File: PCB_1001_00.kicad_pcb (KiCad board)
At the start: 2 copper layers, 37.6 x 30.7 mm, 4 parts, among them SW1 SW_MEC_5G

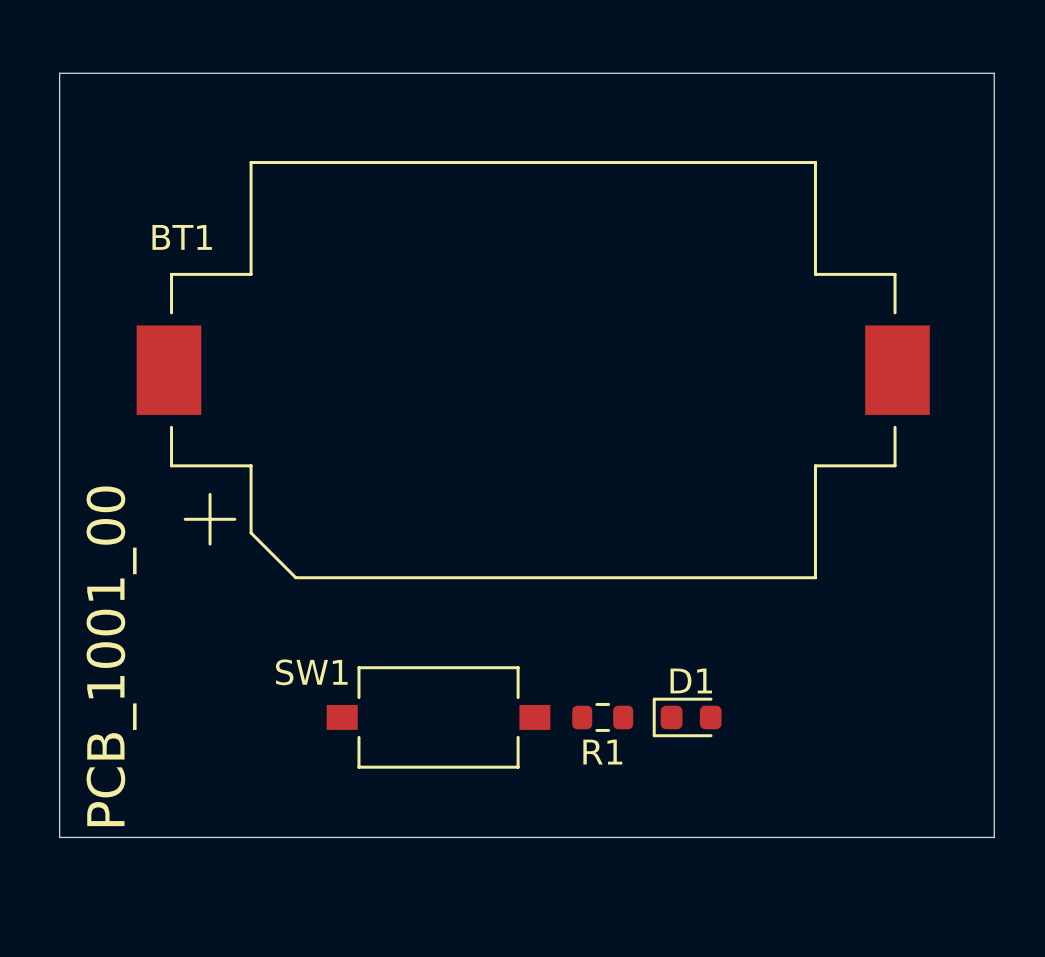
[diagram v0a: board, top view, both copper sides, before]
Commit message: PCB -->01, 2 additional LED circuits
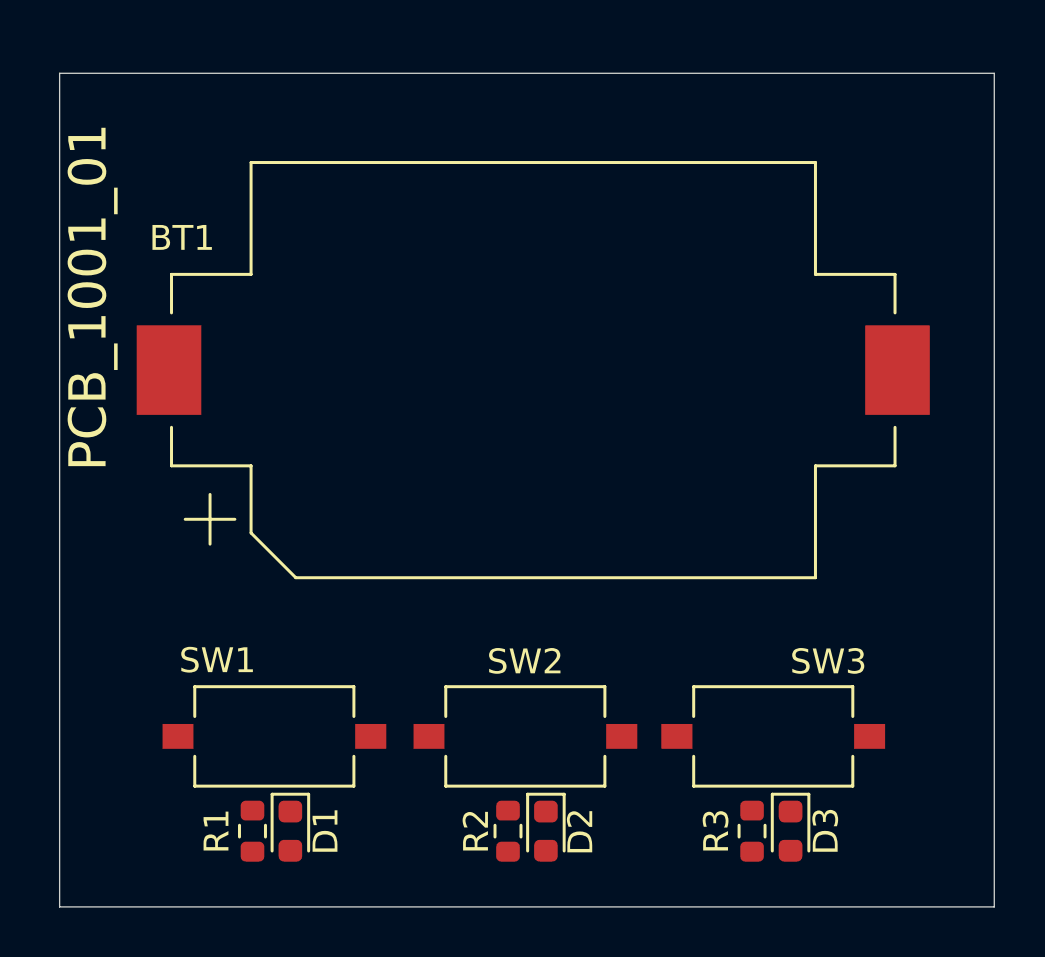
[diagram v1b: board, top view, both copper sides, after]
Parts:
- added D2: LED, LED_SMD:LED_0603_1608Metric, F.Cu at (143.3, 109.0)
- added D3: LED, LED_SMD:LED_0603_1608Metric, F.Cu at (153.1, 109.0)
- added R2: 330R, Resistor_SMD:R_0603_1608Metric, F.Cu at (141.7, 109.0)
- added R3: 330R, Resistor_SMD:R_0603_1608Metric, F.Cu at (151.5, 109.0)
- added SW2: SW_MEC_5G, Button_Switch_SMD:SW_Tactile_SPST_NO_Straight_CK_PTS636Sx25SMTRLFS, F.Cu at (142.4, 105.2)
- added SW3: SW_MEC_5G, Button_Switch_SMD:SW_Tactile_SPST_NO_Straight_CK_PTS636Sx25SMTRLFS, F.Cu at (152.4, 105.2)
- moved D1 16.8 mm to (133.0, 109.0), turned to -90 degrees
- moved R1 14.8 mm to (131.5, 109.0), turned to 90 degrees
- moved SW1 6.65 mm to (132.3, 105.2)
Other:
- board size 37.6 x 30.7 mm -> 37.6 x 33.5 mm
- board text added: "PCB_1001_01"
- board text removed: "PCB_1001_00"

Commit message: PCB_1001_01 routing completed
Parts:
- SW1, SW2, SW3: value SW_MEC_5G -> SW_MEC_5G_edit
- moved SW3 0.76 mm to (153.2, 105.2)
- moved SW2 0.57 mm to (143.0, 105.2)
- moved SW1 0.25 mm to (132.1, 105.2)
- turned R1 to -90 degrees
- turned R2 to -90 degrees
- turned R3 to -90 degrees
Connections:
- SW1 pad 2: Net-(BT1-+) -> Net-(D1-A)
- SW2 pad 2: Net-(D1-A) -> Net-(D2-A)
- SW3 pad 2: Net-(D2-A) -> Net-(D3-A)
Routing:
- net Net-(BT1--): track 0.00 -> 51.6 mm
- net Net-(BT1-+): track 0.00 -> 14.8 mm
- net Net-(D1-A): track 0.00 -> 10.2 mm
- net Net-(D2-A): track 0.00 -> 9.83 mm
- net Net-(D3-A): track 0.00 -> 7.74 mm
- net Net-(D3-K): track 0.00 -> 1.57 mm
- net Net-(D2-K): track 0.00 -> 1.55 mm
- net Net-(D1-K): track 0.00 -> 1.55 mm

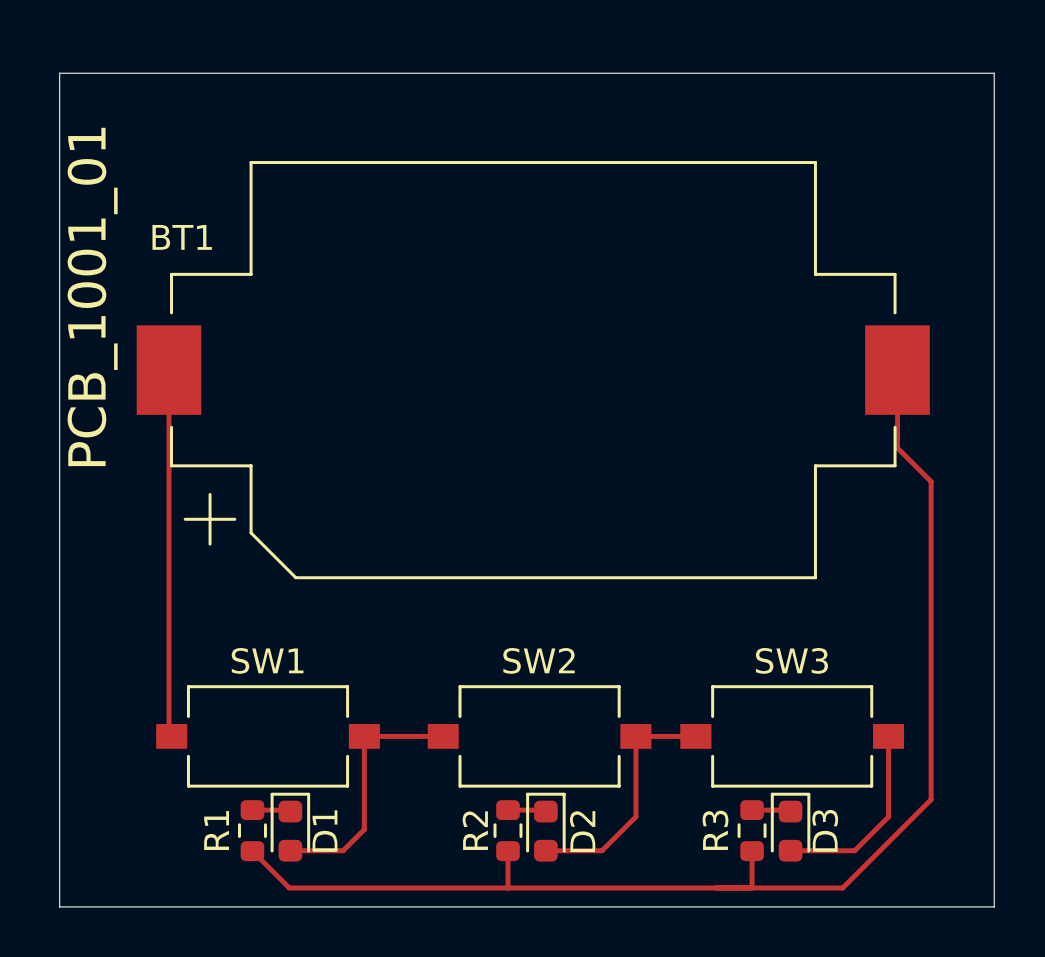
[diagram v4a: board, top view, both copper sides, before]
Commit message: Updated file naming to remove spaces
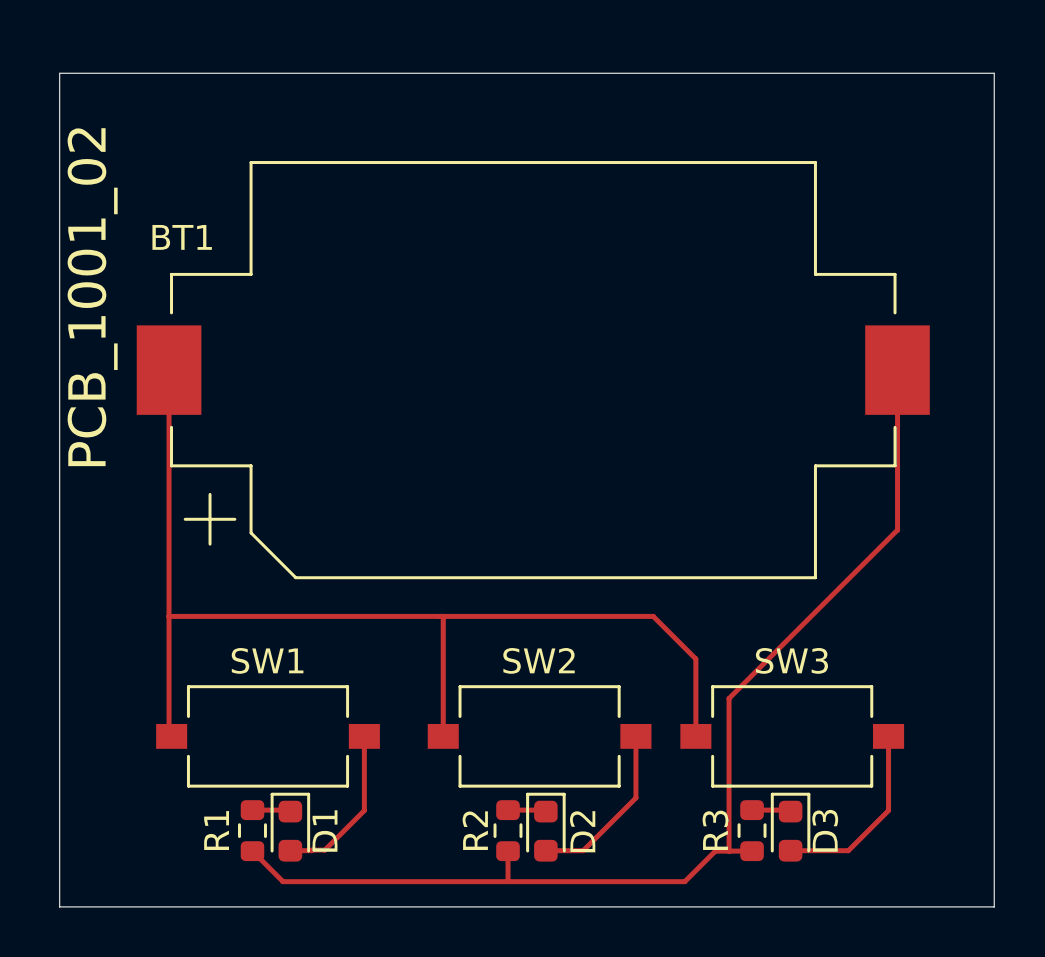
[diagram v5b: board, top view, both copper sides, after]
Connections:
- SW2 pad 1: Net-(D1-A) -> Net-(BT1-+)
- SW3 pad 1: Net-(D2-A) -> Net-(BT1-+)
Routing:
- net Net-(BT1-+): track 14.8 -> 44.9 mm
- net Net-(BT1--): track 51.6 -> 44.5 mm
- net Net-(D1-A): track 10.2 -> 6.63 mm
- net Net-(D2-A): track 9.83 -> 6.98 mm
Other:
- board text added: "PCB_1001_02"
- board text removed: "PCB_1001_01"
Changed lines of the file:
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@@
 		(sheetname "Root")
 		(sheetfile "PCB_1001_00.kicad_sch")
-		(attr smd)
+		(attr smd dnp)
 		(fp_line
 			(start -1.485 0.735)
@@
 		(sheetname "Root")
 		(sheetfile "PCB_1001_00.kicad_sch")
-		(attr smd)
+		(attr smd dnp)
 		(fp_line
 			(start -3.2 -2)
@@
 			(size 1.25 1)
 			(layers "F.Cu" "F.Paste" "F.Mask")
-			(net 3 "Net-(D1-A)")
+			(net 1 "Net-(BT1-+)")
 			(pinfunction "A")
 			(pintype "passive")
@@
 		(sheetname "Root")
 		(sheetfile "PCB_1001_00.kicad_sch")
-		(attr smd dnp)
+		(attr smd)
 		(fp_line
 			(start -1.485 0.735)
@@
 		(sheetname "Root")
 		(sheetfile "PCB_1001_00.kicad_sch")
-		(attr smd dnp)
+		(attr smd)
 		(fp_line
 			(start -3.2 -2)
@@
 			(size 1.25 1)
 			(layers "F.Cu" "F.Paste" "F.Mask")
-			(net 5 "Net-(D2-A)")
+			(net 1 "Net-(BT1-+)")
 			(pinfunction "A")
 			(pintype "passive")
@@
 		(sheetname "Root")
 		(sheetfile "PCB_1001_00.kicad_sch")
-		(attr smd)
+		(attr smd dnp)
 		(fp_line
 			(start -0.237258 0.5225)
@@
 		(sheetname "Root")
 		(sheetfile "PCB_1001_00.kicad_sch")
-		(attr smd dnp)
+		(attr smd)
 		(fp_line
 			(start -0.237258 0.5225)
@@
 		(layer "Edge.Cuts")
 	)
-	(gr_text "PCB_1001_01"
+	(gr_text "PCB_1001_02"
 		(at 125.73 94.488 90)
 		(layer "F.SilkS")
@@
 	)
 	(segment
+		(start 139.192 100.33)
+		(end 139.127 100.395)
+		(width 0.2)
+		(layer "F.Cu")
+		(net 1)
+	)
+	(segment
+		(start 149.287 102.043)
+		(end 149.287 105.156)
+		(width 0.2)
+		(layer "F.Cu")
+		(net 1)
+	)
+	(segment
+		(start 128.098 100.33)
+		(end 128.098 105.049)
+		(width 0.2)
+		(layer "F.Cu")
+		(net 1)
+	)
+	(segment
+		(start 138.938 100.33)
+		(end 147.574 100.33)
+		(width 0.2)
+		(layer "F.Cu")
+		(net 1)
+	)
+	(segment
+		(start 139.127 100.395)
+		(end 139.127 105.156)
+		(width 0.2)
+		(layer "F.Cu")
+		(net 1)
+	)
+	(segment
+		(start 147.574 100.33)
+		(end 149.287 102.043)
+		(width 0.2)
+		(layer "F.Cu")
+		(net 1)
+	)
+	(segment
+		(start 128.098 100.33)
+		(end 138.938 100.33)
+		(width 0.2)
+		(layer "F.Cu")
+		(net 1)
+	)
+	(segment
+		(start 128.098 90.424)
+		(end 128.098 100.33)
+		(width 0.2)
+		(layer "F.Cu")
+		(net 1)
+	)
+	(segment
 		(start 128.098 105.049)
 		(end 128.205 105.156)
@@
 	)
 	(segment
-		(start 128.098 90.424)
-		(end 128.098 105.049)
+		(start 138.938 100.33)
+		(end 139.192 100.33)
 		(width 0.2)
 		(layer "F.Cu")
@@
 	)
 	(segment
-		(start 141.732 111.252)
-		(end 150.114 111.252)
+		(start 141.732 109.771)
+		(end 141.732 110.998)
 		(width 0.2)
 		(layer "F.Cu")
@@
 	)
 	(segment
-		(start 132.936 111.252)
-		(end 141.732 111.252)
+		(start 157.398 96.856)
+		(end 150.622 103.632)
 		(width 0.2)
 		(layer "F.Cu")
@@
 	)
 	(segment
-		(start 141.732 109.771)
-		(end 141.732 111.252)
+		(start 131.455 109.771)
+		(end 132.682 110.998)
 		(width 0.2)
 		(layer "F.Cu")
@@
 	)
 	(segment
-		(start 158.75 107.696)
-		(end 155.194 111.252)
+		(start 150.071 109.771)
+		(end 150.622 109.771)
 		(width 0.2)
 		(layer "F.Cu")
@@
 	)
 	(segment
-		(start 155.194 111.252)
-		(end 150.114 111.252)
+		(start 150.622 109.771)
+		(end 151.5475 109.771)
 		(width 0.2)
 		(layer "F.Cu")
@@
 	)
 	(segment
-		(start 157.398 93.558)
-		(end 158.75 94.91)
+		(start 132.682 110.998)
+		(end 141.732 110.998)
 		(width 0.2)
 		(layer "F.Cu")
@@
 	)
 	(segment
-		(start 158.75 94.91)
-		(end 158.75 107.696)
+		(start 148.844 110.998)
+		(end 150.071 109.771)
 		(width 0.2)
 		(layer "F.Cu")
@@
 	)
 	(segment
-		(start 150.114 111.252)
-		(end 151.5475 111.252)
+		(start 150.622 103.632)
+		(end 150.622 109.771)
 		(width 0.2)
 		(layer "F.Cu")
@@
 	(segment
 		(start 157.398 90.424)
-		(end 157.398 93.558)
+		(end 157.398 96.856)
 		(width 0.2)
 		(layer "F.Cu")
@@
 	)
 	(segment
-		(start 151.5475 111.252)
-		(end 151.5475 109.771)
+		(start 141.732 110.998)
+		(end 148.844 110.998)
 		(width 0.2)
 		(layer "F.Cu")
@@
 	)
 	(segment
-		(start 131.455 109.771)
-		(end 132.936 111.252)
-		(width 0.2)
-		(layer "F.Cu")
-		(net 2)
-	)
-	(segment
-		(start 132.979 109.7535)
-		(end 135.1025 109.7535)
+		(start 133.8325 109.7535)
+		(end 132.979 109.7535)
 		(width 0.2)
 		(layer "F.Cu")
@@
 	)
 	(segment
+		(start 134.366 109.728)
+		(end 133.858 109.728)
+		(width 0.2)
+		(layer "F.Cu")
+		(net 3)
+	)
+	(segment
+		(start 133.858 109.728)
+		(end 133.8325 109.7535)
+		(width 0.2)
+		(layer "F.Cu")
+		(net 3)
+	)
+	(segment
+		(start 135.955 108.139)
+		(end 134.366 109.728)
+		(width 0.2)
+		(layer "F.Cu")
+		(net 3)
+	)
+	(segment
 		(start 135.955 105.156)
-		(end 139.127 105.156)
+		(end 135.955 108.139)
 		(width 0.2)
 		(layer "F.Cu")
@@
 	)
 	(segment
-		(start 135.1025 109.7535)
-		(end 135.955 108.901)
-		(width 0.2)
-		(layer "F.Cu")
-		(net 3)
-	)
-	(segment
-		(start 135.955 108.901)
-		(end 135.955 105.156)
-		(width 0.2)
-		(layer "F.Cu")
-		(net 3)
+		(start 132.9215 108.121)
+		(end 132.979 108.1785)
+		(width 0.2)
+		(layer "F.Cu")
+		(net 4)
 	)
 	(segment
@@
 	)
 	(segment
-		(start 132.9215 108.121)
-		(end 132.979 108.1785)
-		(width 0.2)
-		(layer "F.Cu")
-		(net 4)
+		(start 144.7545 109.7535)
+		(end 146.877 107.631)
+		(width 0.2)
+		(layer "F.Cu")
+		(net 5)
+	)
+	(segment
+		(start 146.877 107.631)
+		(end 146.877 105.156)
+		(width 0.2)
+		(layer "F.Cu")
+		(net 5)
 	)
 	(segment
 		(start 143.256 109.7535)
-		(end 145.5165 109.7535)
-		(width 0.2)
-		(layer "F.Cu")
-		(net 5)
-	)
-	(segment
-		(start 146.877 105.156)
-		(end 149.287 105.156)
-		(width 0.2)
-		(layer "F.Cu")
-		(net 5)
-	)
-	(segment
-		(start 146.877 108.393)
-		(end 146.877 105.156)
-		(width 0.2)
-		(layer "F.Cu")
-		(net 5)
-	)
-	(segment
-		(start 145.5165 109.7535)
-		(end 146.877 108.393)
+		(end 144.7545 109.7535)
 		(width 0.2)
 		(layer "F.Cu")
@@
 	)
 	(segment
-		(start 157.037 108.393)
-		(end 155.6765 109.7535)
+		(start 155.4225 109.7535)
+		(end 157.037 108.139)
 		(width 0.2)
 		(layer "F.Cu")
@@
 	)
 	(segment
-		(start 157.037 105.156)
-		(end 157.037 108.393)
+		(start 153.097 109.7535)
+		(end 155.4225 109.7535)
 		(width 0.2)
 		(layer "F.Cu")
@@
 	)
 	(segment
-		(start 155.6765 109.7535)
-		(end 153.097 109.7535)
-		(width 0.2)
-		(layer "F.Cu")
+		(start 157.037 108.139)
+		(end 157.037 105.156)
+		(width 0.2)
+		(layer "F.Cu")
